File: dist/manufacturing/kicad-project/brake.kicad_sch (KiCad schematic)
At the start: 39 parts, among them J3 B2P-VH(LF)(SN), Q16 CSD19534Q5A, U12 TL431AIDBZR, U13 TLV3201AIDBVR, U14 TLV3201AIDBVR, U15 UCC27511DBVR

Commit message: Complete orderable PD1180-EPR board release
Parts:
- removed GND (x10): GND, symbol Custom:rail_down
- removed Q16: CSD19534Q5A, symbol Device:U_CSD19534Q5A
- removed TMC_12V (x2): TMC_12V, symbol Custom:rail_up
- removed V3V3 (x3): V3V3, symbol Custom:rail_up
- removed VMOTOR (x3): VMOTOR, symbol Custom:rail_up
- added GND (x10): GND, symbol Custom:rail_down
- added Q16: Q16, symbol Custom:CSD19534Q5A_POWER_NMOS
- added TMC_12V (x2): TMC_12V, symbol Custom:rail_up
- added V3V3 (x4): V3V3, symbol Custom:rail_up
- added VMOTOR (x3): VMOTOR, symbol Custom:rail_up
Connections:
- net at R64.1: now also VMOTOR.1
- net at R65.1: now also U14.4 (IN_NEG); no longer R64.2
- net at R68.1: now also U15.2 (OUTH), U15.3 (OUTL)
- net BRAKE_GATE: now reaches R68.2, R69.1
- net at C41.2: now also GND.1; no longer R66.2
- net at U13.2 (GND): now also GND.1
- net at C40.1, U13.5 (VCC): now also V3V3.1
- net at C40.2, R62.2: now also GND.1
- net at R60.1: now also VMOTOR.1
- net at R59.1: now also V3V3.1
- net at C41.1: now also V3V3.1; no longer U14.5 (VCC)
- net at R69.2: now also GND.1
- net at U12.3 (ANODE): now also GND.1
- net at R67.2: now also U14.2 (GND), GND.1
- net at U15.1 (VDD): now also TMC_12V.1
- net at U15.4 (GND), U15.5 (IN_NEG): now also GND.1
- net at C42.1, C43.1: now also TMC_12V.1
- net at J3.1: now also VMOTOR.1
- net at C42.2, C43.2: now also GND.1
- net VMOTOR_OK: no longer names the net of R67.1
- new net: GND.1, R66.2
- new net: GND.1, Q16.1 (source), Q16.2 (S2), Q16.3 (S3)
- new net: U14.5 (VCC), V3V3.1
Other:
- note added: "U12: precision threshold reference. U13/U14: overvoltage comparators. U15: MOSFET gate driver. Q16: brake switch."

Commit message: Fix schematic style and top-side reset switch
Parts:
- removed GND (x10): GND, symbol Custom:rail_down
- removed TMC_12V (x2): TMC_12V, symbol Custom:rail_up
- removed V3V3 (x4): V3V3, symbol Custom:rail_up
- removed VMOTOR (x3): VMOTOR, symbol Custom:rail_up
- added GND (x10): GND, symbol Custom:rail_down
- added TMC_12V (x2): TMC_12V, symbol Custom:rail_up
- added V3V3 (x4): V3V3, symbol Custom:rail_up
- added VMOTOR (x3): VMOTOR, symbol Custom:rail_up
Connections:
- net at C41.2: now also GND.1
- net at R66.2: now also GND.1
- net at R67.2, U14.2 (GND): now also GND.1
- net at U13.2 (GND): now also GND.1
- net at R69.2: now also GND.1
- net at C42.1, C43.1: now also TMC_12V.1
- net at C42.2, C43.2: now also GND.1
- net at C40.2, R62.2: now also GND.1
- net at R59.1: now also V3V3.1
- net at U15.4 (GND), U15.5 (IN_NEG): now also GND.1
- net at Q16.1 (S1), Q16.2 (S2), Q16.3 (S3): now also GND.1
- net at C41.1: now also V3V3.1
- net at C40.1, U13.5 (VCC): now also V3V3.1
- net at U12.3 (ANODE): now also GND.1
- net at U14.5 (VCC): now also V3V3.1
- net at R60.1: now also VMOTOR.1
- net BRAKE_SENSE: now reaches R62.1
- net BRAKE_SENSE: now also R61.2
- net at R63.1: now also U13.1 (OUT)
- net at U13.3 (IN_POS): no longer R61.2
- net at J3.1: now also VMOTOR.1
- net at R64.1: now also VMOTOR.1
- net at U15.1 (VDD): now also TMC_12V.1

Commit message: Use one USB-C port for PD and data
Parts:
- removed GND (x10): GND, symbol Custom:rail_down
- removed TMC_12V (x2): TMC_12V, symbol Custom:rail_up
- removed V3V3 (x4): V3V3, symbol Custom:rail_up
- removed VMOTOR (x3): VMOTOR, symbol Custom:rail_up
- added GND (x10): GND, symbol Custom:rail_down
- added TMC_12V (x2): TMC_12V, symbol Custom:rail_up
- added V3V3 (x4): V3V3, symbol Custom:rail_up
- added VMOTOR (x3): VMOTOR, symbol Custom:rail_up
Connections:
- net at R64.1: now also VMOTOR.1
- net at R59.1: now also V3V3.1
- net at R69.2: now also GND.1
- net at C41.1: now also V3V3.1
- net at C42.1, C43.1: now also TMC_12V.1
- net at C42.2, C43.2: now also GND.1
- net at U14.5 (VCC): now also V3V3.1
- net at U15.1 (VDD): now also TMC_12V.1
- net at U15.4 (GND), U15.5 (IN_NEG): now also GND.1
- net at R60.1: now also VMOTOR.1
- net at C40.2, R62.2: now also GND.1
- net at R67.2, U14.2 (GND): now also GND.1
- net at U12.3 (ANODE): now also GND.1
- net at J3.1: now also VMOTOR.1
- net at R66.2: now also GND.1
- net at U13.2 (GND): now also GND.1
- net at Q16.1 (S1), Q16.2 (S2), Q16.3 (S3): now also GND.1
- net at C40.1, U13.5 (VCC): now also V3V3.1
- net at C41.2: now also GND.1

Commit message: fix: finalize single-port EPR controller
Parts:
- removed GND (x10): GND, symbol Custom:rail_down
- removed TMC_12V (x2): TMC_12V, symbol Custom:rail_up
- removed V3V3 (x4): V3V3, symbol Custom:rail_up
- removed VMOTOR (x3): VMOTOR, symbol Custom:rail_up
- C40, C41, C42, C43: footprint (none) -> capacitor_cap0603
- J3: value B2P-VH(LF)(SN) -> J3; footprint (none) -> B2P-VH_LF_SN
- Q16: footprint (none) -> CSD19534Q5A
- R59, R60, R61, R62, R63, R64, R65, R66, R67, R68, R69: footprint (none) -> resistor_res0603
- U12: footprint (none) -> TL431AIDBZR
- U13, U14: footprint (none) -> TLV3201AIDBVR
- U15: footprint (none) -> UCC27511DBVR
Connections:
- net BRAKE_GATE: now also Q16.4 (G)
- net BRAKE_SENSE: now also R63.2, U13.3 (IN_POS)
- net TMC_12V: now reaches C42.1, C43.1
- net TMC_12V: now also U15.1 (VDD)
- net GND: now reaches C42.2, C43.2
- net GND: now also C40.2, C41.2, Q16.1 (S1), Q16.2 (S2), Q16.3 (S3), R62.2, R66.2, R67.2, R69.2, U12.3 (ANODE), U13.2 (GND), U14.2 (GND), U15.4 (GND), U15.5 (IN_NEG)
- net V3V3: now reaches C40.1, U13.5 (VCC)
- net V3V3: now also C41.1, R59.1, U14.5 (VCC)
- net MOTOR_OVP_SENSE: now reaches R65.1, U14.4 (IN_NEG)
- net MOTOR_OVP_SENSE: now also R64.2
- net MOTOR_OVP_LOW: now reaches R65.2
- net MOTOR_OVP_LOW: now also R66.1
- net VMOTOR: now reaches R64.1
- net VMOTOR: now also J3.1, R60.1
- net VREF_2V495: now reaches R59.2
- net VREF_2V495: now also U12.1 (CATHODE), U12.2 (REF), U13.4 (IN_NEG), U14.3 (IN_POS)
- net BRAKE_ON: now reaches R63.1, U13.1 (OUT)
- net BRAKE_ON: now also U15.6 (IN_POS)
- net VMOTOR_OK: now reaches U14.1 (OUT)
- net VMOTOR_OK: now also R67.1
- net BRAKE_DRIVE: now reaches R68.1, U15.2 (OUTH), U15.3 (OUTL)
- net BRAKE_MID: now reaches R61.1
- net BRAKE_MID: now also R60.2
- net BRAKE_RETURN: now reaches J3.2
- net BRAKE_RETURN: now also Q16.5 (D1), Q16.6 (D2), Q16.7 (D3), Q16.8 (D4), Q16.9 (D5)

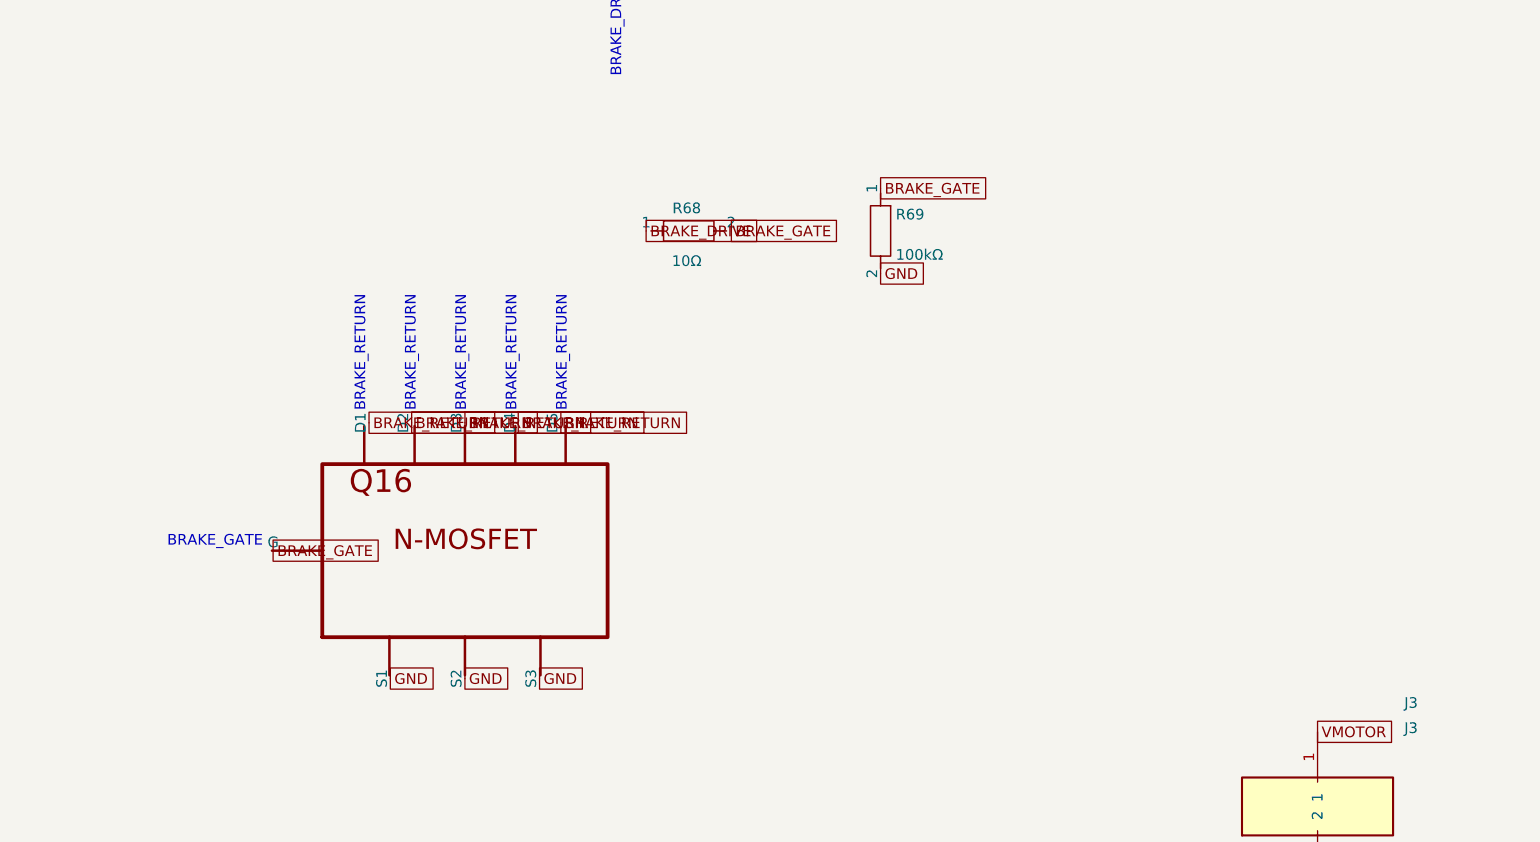
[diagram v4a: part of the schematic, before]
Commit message: Implement dual USB power/data ECO and consolidate industrial I/O
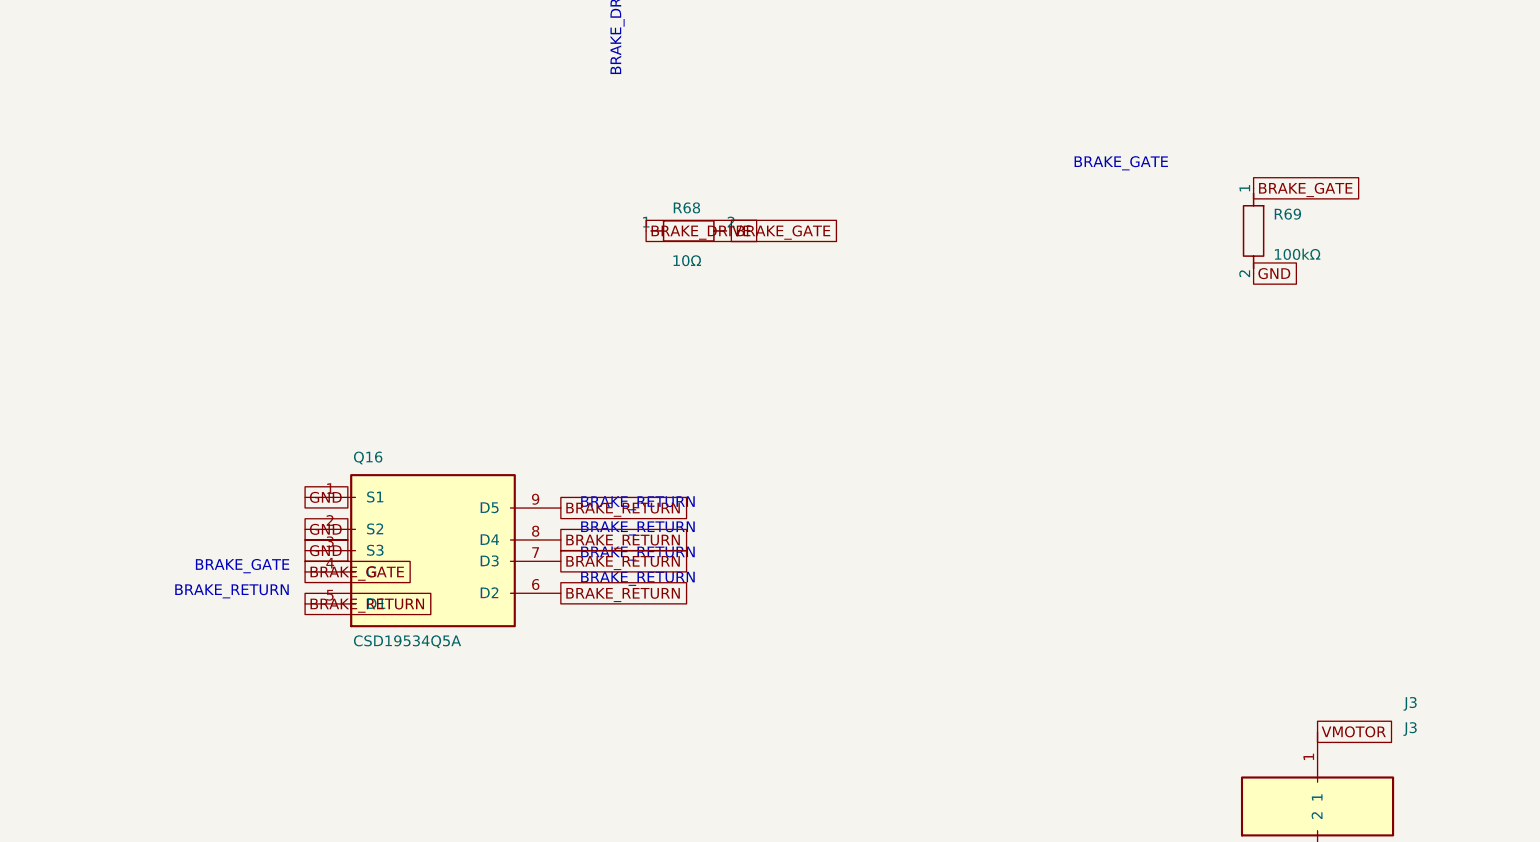
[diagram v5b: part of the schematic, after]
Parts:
- removed Q16: Q16, CSD19534Q5A, symbol Custom:CSD19534Q5A_POWER_NMOS
- added Q16: CSD19534Q5A, CSD19534Q5A, symbol Device:U_CSD19534Q5A
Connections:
- net BRAKE_GATE: now also Q16.4 (G)
- net BRAKE_RETURN: now also Q16.5 (D1), Q16.6 (D2), Q16.7 (D3), Q16.8 (D4), Q16.9 (D5)
- net GND: now also Q16.1 (S1), Q16.2 (S2), Q16.3 (S3)
